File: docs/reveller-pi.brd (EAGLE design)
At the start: 85.1 x 55.9 mm, 22 parts, among them IC100 6581, Q100 IRF9Z24N, T100 BC547, X100 RASPI_BOARD_AB_E0, X101 PG203J, X102 CANTON-POWER

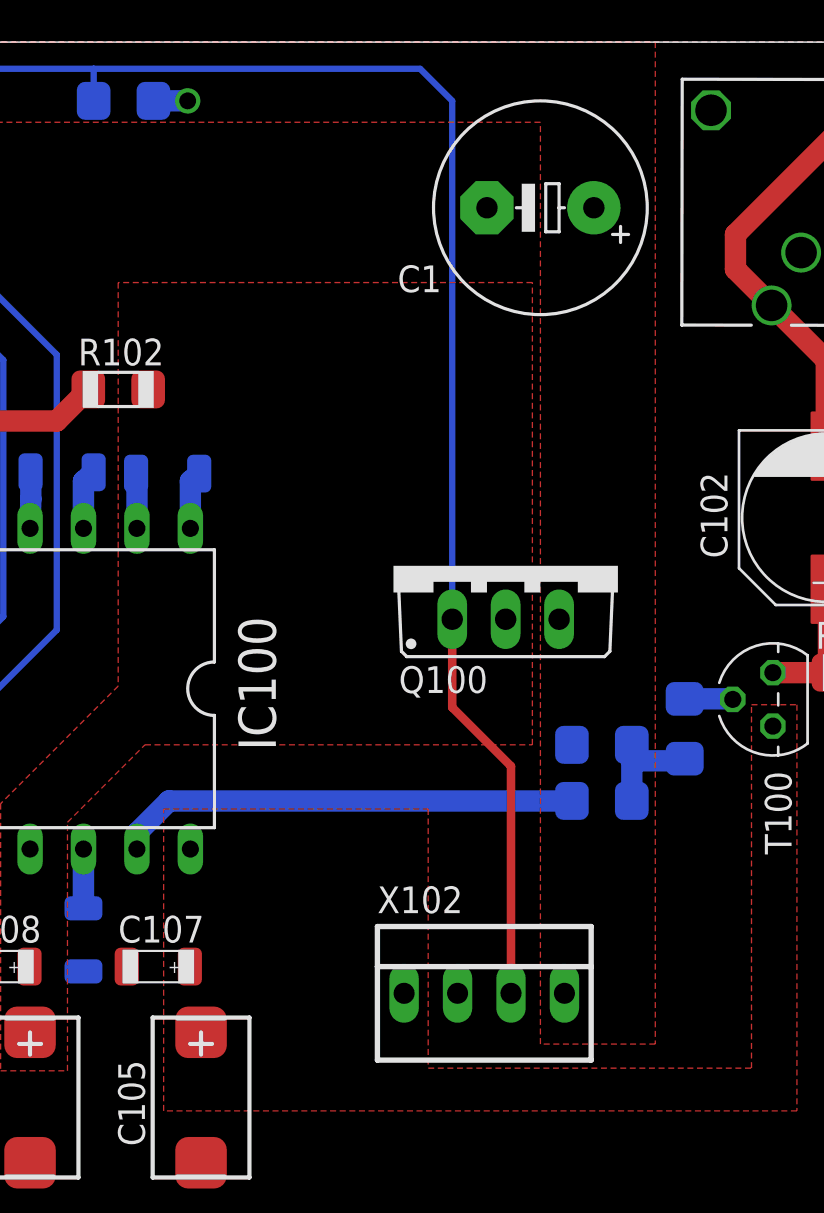
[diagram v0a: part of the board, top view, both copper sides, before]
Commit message: replaced cap with resistor
Switched out Capacitor with resistors as its better.
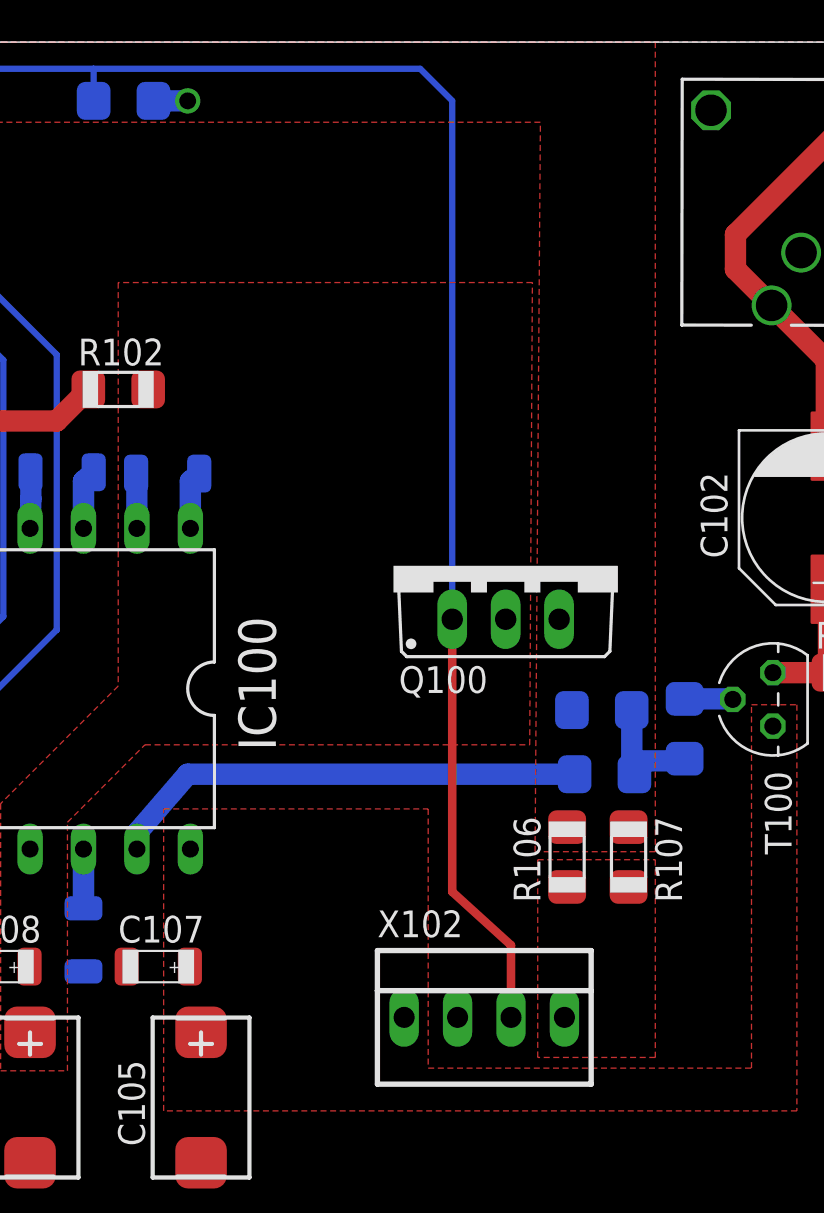
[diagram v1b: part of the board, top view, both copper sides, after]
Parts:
- removed C1: 1000uF, rcl:E5-10,5
- added R106, R107: 4.7, cyviz:SMD-IPC_R1206
- moved R100 1.65 mm to (62.7, 24.1)
- moved R103 1.28 mm to (62.9, 21.1)
- moved X102 1.14 mm to (57.1, 9.53)
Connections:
- new net N$1: R106.1, R107.1, X102.4
- net +5V: now also R106.2, R107.2; no longer C1.+, X102.4
- net GND: no longer C1.-
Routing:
- net PWCTL: track 87.0 -> 88.2 mm
- net AUDIO_RAW: track 22.1 -> 22.8 mm
- net N$1: track 0.00 -> 0.58 mm
- added copper zone on layer 1, net N$2
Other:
- board text added: "Reveller Sid Player #FluXxX V0.2"
- board text removed: "Reveller Sid Player #FluXxX V0.1"
